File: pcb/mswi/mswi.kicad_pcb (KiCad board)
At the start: 2 copper layers, 140 x 72.3 mm, 153 parts, among them J301 ISP, J302 USART, J303 I2C, J501 Conn_01x04_Male, Q301 BC856, Q401 BC856, Q402 BC856, Q403 BC856, Q404 BC856, Q405 BC856, Q406 BC856, Q407 BC856, Q408 BC856, Q409 BC856, Q410 BC856, Q411 BC856, Q412 BC856, Q413 BC856, Q414 BC856, Q415 BC856, Q416 BC856, Q417 BC856, Q418 BC856, Q419 BC856, Q420 BC856, Q601 si2308cds, SW401 SW_Push, SW402 SW_Push, SW403 SW_Push, SW404 SW_Push, SW405 SW_Push, SW406 SW_Push, SW407 SW_Push, SW408 SW_Push, SW409 SW_Push, SW410 SW_Push, U201 MCP2551-I/SN, U202 MCP2515-xSO, U301 ATmega328PB-AU, U601 LM7805, Y201 16MHz, Y301 16MHz

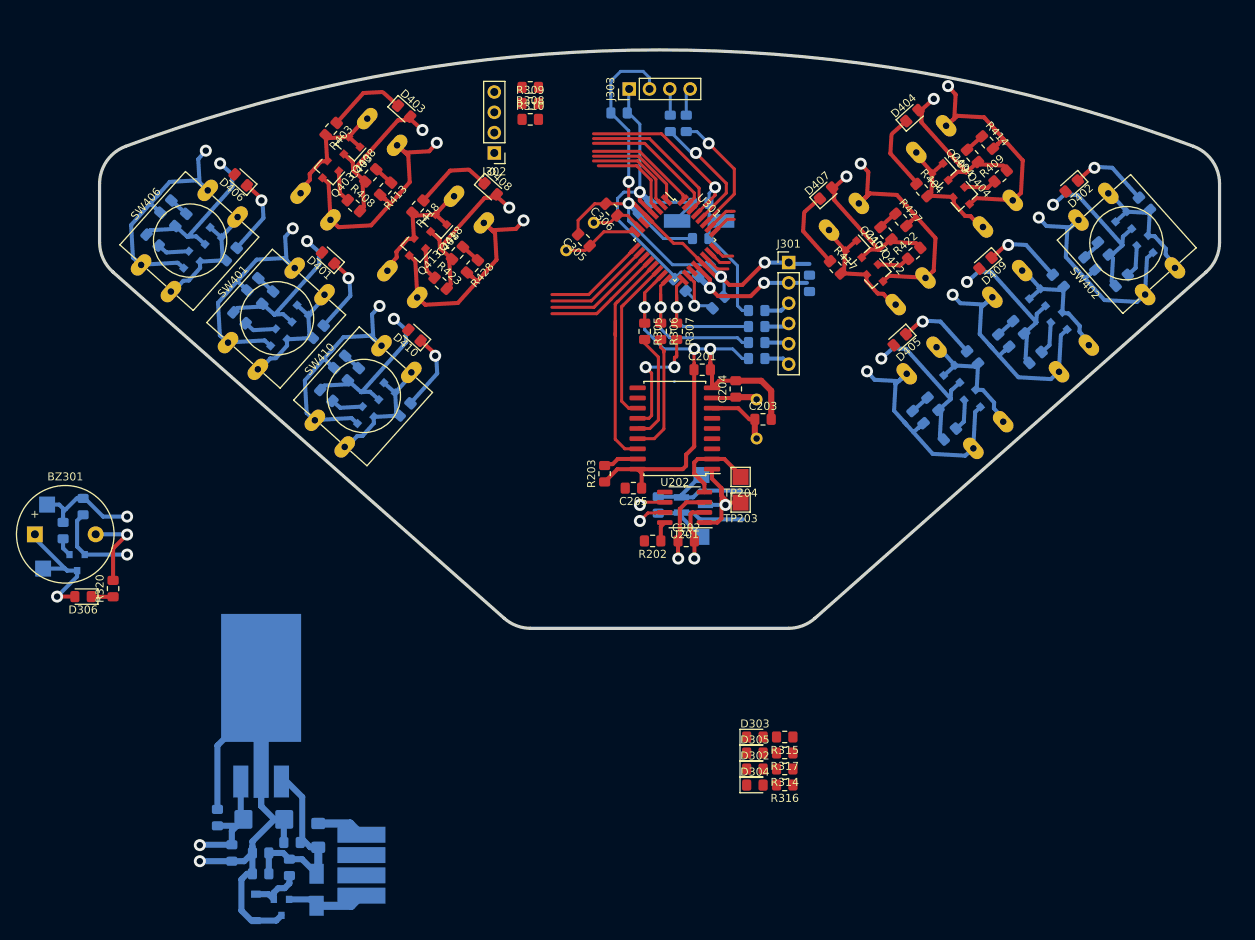
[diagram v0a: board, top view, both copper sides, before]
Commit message: Routing done. Needs rework to fabrication
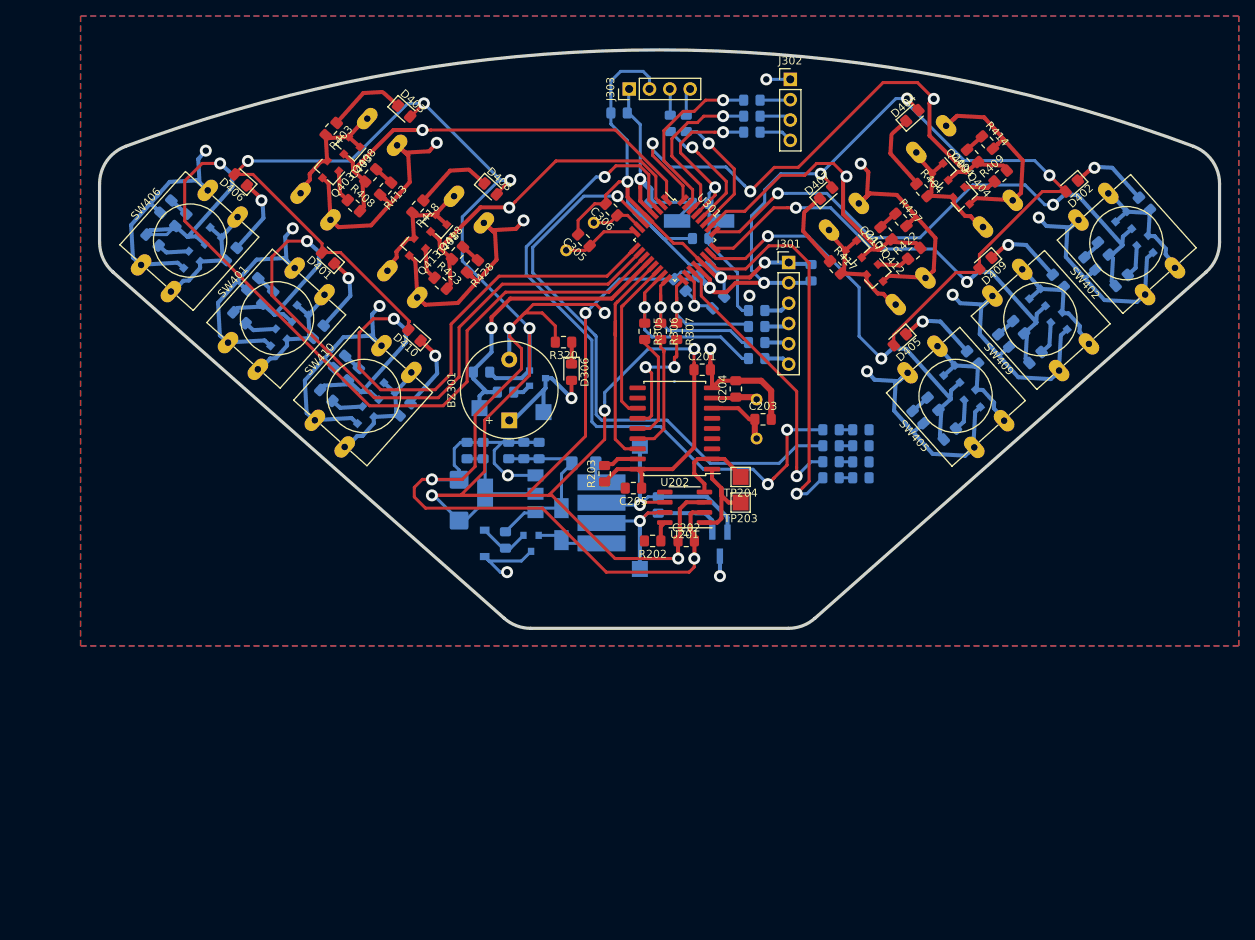
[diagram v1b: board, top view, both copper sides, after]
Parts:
- D302, D303, D304, D305, R308, R309, R310, R314, R315, R316, R317: moved to B.Cu
- SW405, SW409: moved to F.Cu
- U601: value LM7805 -> LM1117-5.0; footprint KicadZeniteSolarLibrary18:TO-220-3_Horizontal_TabDown_SMD -> Package_TO_SOT_SMD:SOT-223-3_TabPin2
- moved D306 67.2 mm to (134.3, 91.2), turned to 270 degrees
- moved TP307 65.5 mm to (130.8, 96.2), turned to 90 degrees
- moved R320 64.2 mm to (133.3, 87.4), turned to 180 degrees
- moved Q301 62.0 mm to (130.1, 91.9), turned to 0 degrees
- moved C603 61.3 mm to (126.5, 101.0), turned to 90 degrees
- moved BZ301 61.0 mm to (126.6, 97.2), turned to 90 degrees
- moved C601 60.1 mm to (128.4, 101.0), turned to 90 degrees
- moved C604 59.3 mm to (123.3, 101.0), turned to 90 degrees
- moved R319 57.9 mm to (126.1, 93.7), turned to 0 degrees
- moved C602 57.9 mm to (130.3, 101.0), turned to 90 degrees
- moved F601 57.1 mm to (135.9, 102.6), turned to 180 degrees
- moved C605 55.5 mm to (121.3, 101.0)
- moved TP306 55.4 mm to (122.8, 95.7), turned to 90 degrees
- moved Q601 55.2 mm to (129.3, 112.6)
- moved D602 55.0 mm to (133.1, 110.2)
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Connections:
- U301 pad 1: /MCU/SW1 -> /MCU/SW2
- U301 pad 10: /MCU/SW4 -> /MCU/SW0
- U301 pad 2: /MCU/SW2 -> /MCU/SW7
- U301 pad 23: /MCU/SW6 -> /MCU/SW4
- U301 pad 24: /MCU/SW7 -> /MCU/SW8
- U301 pad 25: /MCU/SW8 -> /MCU/SW1
- U301 pad 26: /MCU/SW9 -> /MCU/SW6
- U301 pad 32: /MCU/SW0 -> /MCU/SW3
- U301 pad 9: /MCU/SW3 -> /MCU/SW9
- U601 pad 1: /POWER SUPPLY/+18V -> GND
- U601 pad 2: GND -> +5V
- U601 pad 3: +5V -> /POWER SUPPLY/+18V
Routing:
- net +5V: track 131.3 -> 465.8 mm, vias 7 -> 15
- net /MCU/SW5: track 34.2 -> 112.9 mm
- net /MCU/LED0: track 11.3 -> 87.5 mm, vias 0 -> 3
- net /MCU/LED1: track 0.00 -> 73.9 mm, vias 0 -> 1
- net /MCU/SW0: track 34.2 -> 92.5 mm
- net GND: track 534.5 -> 590.1 mm, vias 19 -> 22
- net /MCU/SW9: track 24.0 -> 76.2 mm
- net /MCU/LED3: track 3.38 -> 49.2 mm, vias 0 -> 1
- net /MCU/SW3: track 32.9 -> 72.7 mm, vias 1 -> 3
- net /MCU/SW1: track 32.7 -> 70.5 mm, vias 1 -> 2
- net /MCU/LED2: track 0.00 -> 35.1 mm, vias 0 -> 1
- net /MCU/SW8: track 23.2 -> 57.6 mm, vias 1 -> 2
- net /MCU/SW2: track 32.4 -> 54.5 mm
- net /MCU/SW7: track 22.8 -> 44.4 mm
- net /MCU/SW4: track 33.6 -> 52.9 mm, vias 1 -> 2
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- added copper zone on B.Cu, net GND
- added copper zone on F.Cu, net GND

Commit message: Rules adapted to the manufactoring method (CNC)
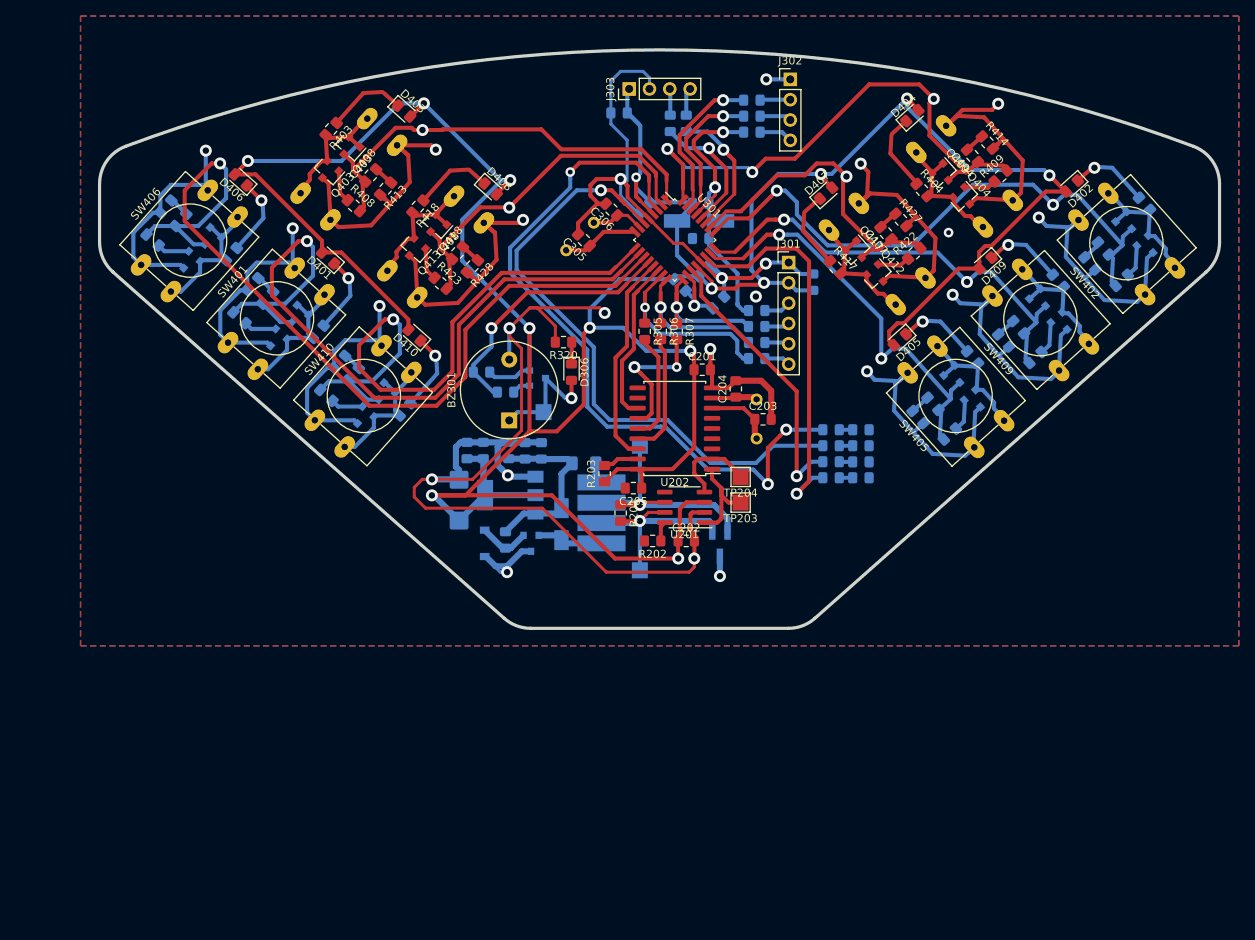
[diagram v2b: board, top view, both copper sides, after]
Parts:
- removed TP306: BUZZ_in, TestPoint:TestPoint_Pad_2.0x2.0mm
- R201: moved to F.Cu
- moved R201 4.81 mm to (140.5, 108.8)
- moved C303 1.20 mm to (164.5, 79.9)
- moved C602 0.29 mm to (130.6, 101.0)
- moved U601 0.17 mm to (126.7, 106.6)
- moved TP207 0.17 mm to (142.9, 116.0)
- moved C601 0.17 mm to (128.6, 101.0)
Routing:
- net +5V: track 465.8 -> 477.9 mm, vias 15 -> 14
- net /CANBUS/SO: track 15.3 -> 25.6 mm
- net GND: track 590.1 -> 580.1 mm, vias 22 -> 24
- net /POWER SUPPLY/+18V: track 22.5 -> 30.7 mm
- net /MCU/SW3: track 72.7 -> 66.5 mm
- net /MCU/SPI_SCK_: track 17.8 -> 22.3 mm
- net Net-(C305-Pad1): track 9.55 -> 13.4 mm
- net /MCU/BUZZER: track 37.2 -> 33.5 mm
- net /MCU/LED0: track 87.5 -> 91.1 mm
- net /MCU/USART_TX: track 22.6 -> 19.5 mm
- net /MCU/SW5: track 112.9 -> 109.9 mm
- net /CANBUS/CS: track 29.5 -> 26.5 mm
- net /MCU/SW1: track 70.5 -> 73.3 mm
- net /MCU/LED1: track 73.9 -> 76.5 mm
- net /MCU/USART_RX: track 20.9 -> 18.4 mm
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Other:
- net class Default: clearance 0.127 -> 0.3048; via_dia 1.5 -> 1.2; via_drill 0.8 -> 0.6
- rule trace_clearance: 0.127 -> 0.3048
- rule trace_min: 0.2 -> 0.381
- rule via_min_drill: 0.3 -> 0.6
- rule via_min_size: 0.4 -> 1.2
- board text added: "TODO: [x] Adapt Rules to Fabrication Method [x] ISP: Change to VERTICAL Version [x] OLED: Footprint & 3D [_] SW: 3D [_] RJ45: 3D [_] Fuse: 3D [x] PCB Geometry [_] Add zenitesolar and designer identification [_] Add opensource hardware symbol [_] Define the switches position -> paper prototype"
- board text removed: "TODO: [_] Adapt Rules to Fabrication Method [x] ISP: Change to VERTICAL Version [x] OLED: Footprint & 3D [_] SW: 3D [_] RJ45: 3D [_] Fuse: 3D [x] PCB Geometry [_] Add zenitesolar and designer identification [_] Add opensource hardware symbol [_] Define the switches position -> paper prototype"

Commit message: SW 3D added
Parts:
- moved C205 0.75 mm to (141.8, 105.0), turned to 0 degrees
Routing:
- net /CANBUS/SO: track 25.6 -> 15.7 mm
- net GND: track 580.1 -> 584.9 mm, vias 24 -> 25
- net Net-(C305-Pad1): track 13.4 -> 10.1 mm
- net /MCU/SW4: track 52.4 -> 54.9 mm
- net /CANBUS/SCK: track 17.4 -> 15.8 mm
- net /MCU/SW5: track 109.9 -> 108.9 mm
- net /MCU/SPI_MOSI_: track 28.2 -> 27.5 mm
- net /CANBUS/RXCAN: track 11.3 -> 10.6 mm
- net Net-(BZ301-Pad1): track 15.6 -> 14.9 mm
- net /MCU/SW1: track 73.3 -> 72.7 mm
- net /MCU/LED3: track 48.8 -> 49.3 mm
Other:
- board text added: "TODO: [x] Adapt Rules to Fabrication Method [x] ISP: Change to VERTICAL Version [x] OLED: Footprint & 3D [x] SW: 3D [_] Fuse: 3D [x] PCB Geometry [_] Add zenitesolar and designer identification [_] Add opensource hardware symbol [_] Define the switches position -> paper prototype"
- board text removed: "TODO: [x] Adapt Rules to Fabrication Method [x] ISP: Change to VERTICAL Version [x] OLED: Footprint & 3D [_] SW: 3D [_] RJ45: 3D [_] Fuse: 3D [x] PCB Geometry [_] Add zenitesolar and designer identification [_] Add opensource hardware symbol [_] Define the switches position -> paper prototype"
